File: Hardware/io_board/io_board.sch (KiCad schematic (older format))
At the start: 74 parts, among them J1 Valves, J10 ADC_VDIV, J11 12V IN, J12 CAN, J13 AS5047, J15 CAN, J2 Valves, J3 Valves, J4 Steering, J5 Steering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

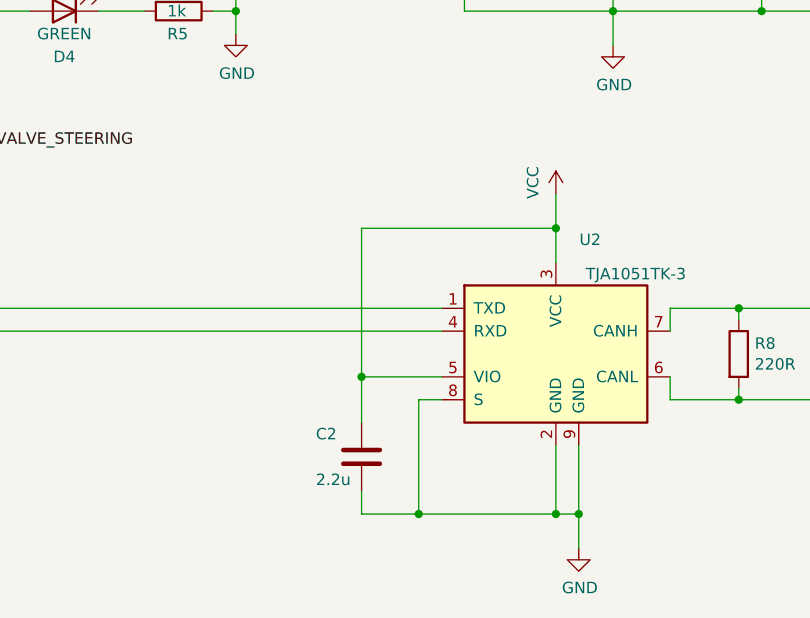
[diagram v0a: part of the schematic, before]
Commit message: Added io_board fw and fixed io_board hw bug
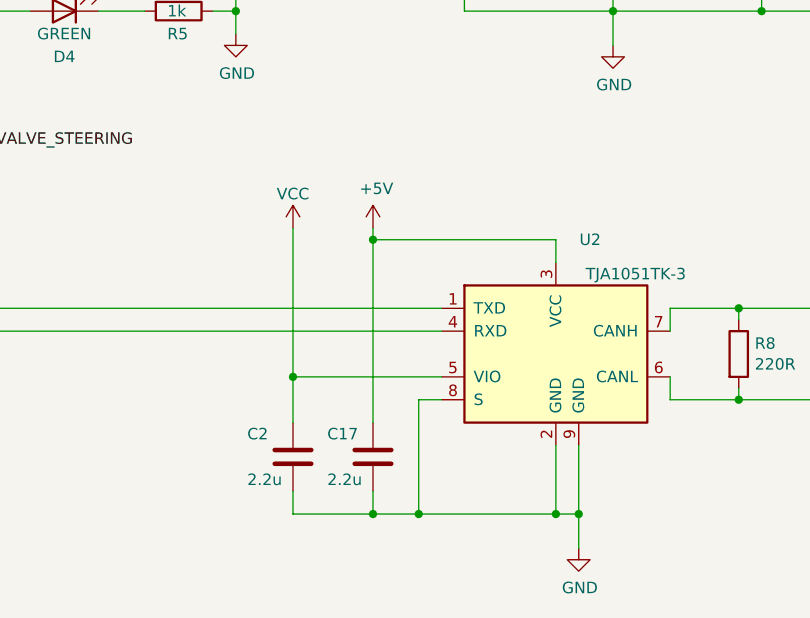
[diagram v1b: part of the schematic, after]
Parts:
- added C17: 2.2u, Capacitor_SMD:C_0603_1608Metric, symbol Device:C
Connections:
- net +5V: now also U2.3 (VCC), C17.1
- net GND: now also C17.2
- net VCC: no longer U2.3 (VCC)
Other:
- moved on the sheet: C2
